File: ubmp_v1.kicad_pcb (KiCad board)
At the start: 2 copper layers, 33.5 x 14 mm, 26 parts, among them J1 Conn_02x05_Counter_Clockwise, J2 USB_A, U1 NUF8401MNT4G, U2 MIC5245-3.3, U3 STM32F103CBUx, U4 NUF2042XV6T1G, Y1 PRQC8.00CR1010V00L

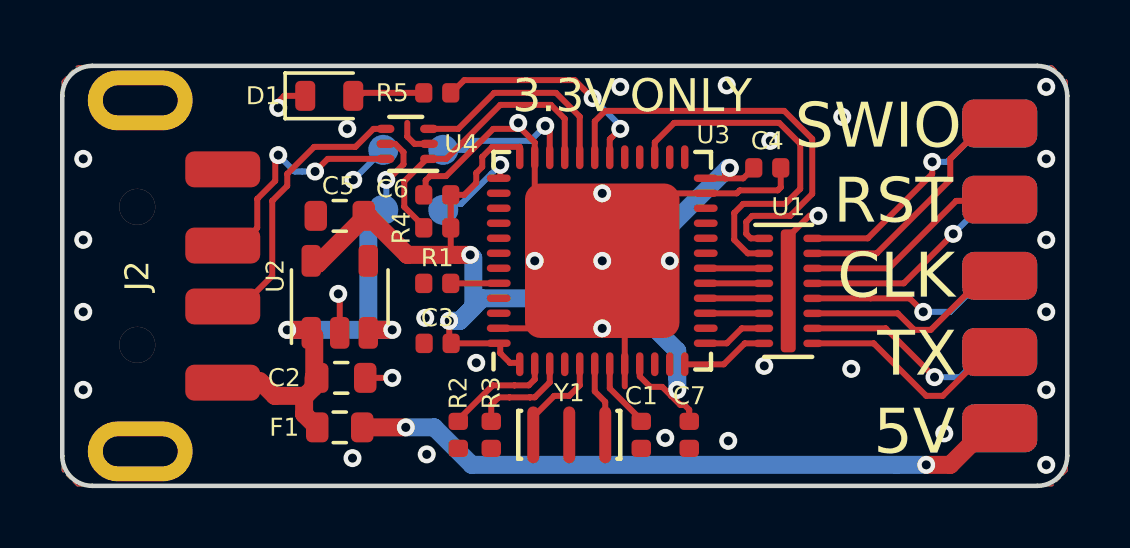
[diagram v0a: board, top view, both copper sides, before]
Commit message: Updated components + libs and changed to 1.5k resistor arrary
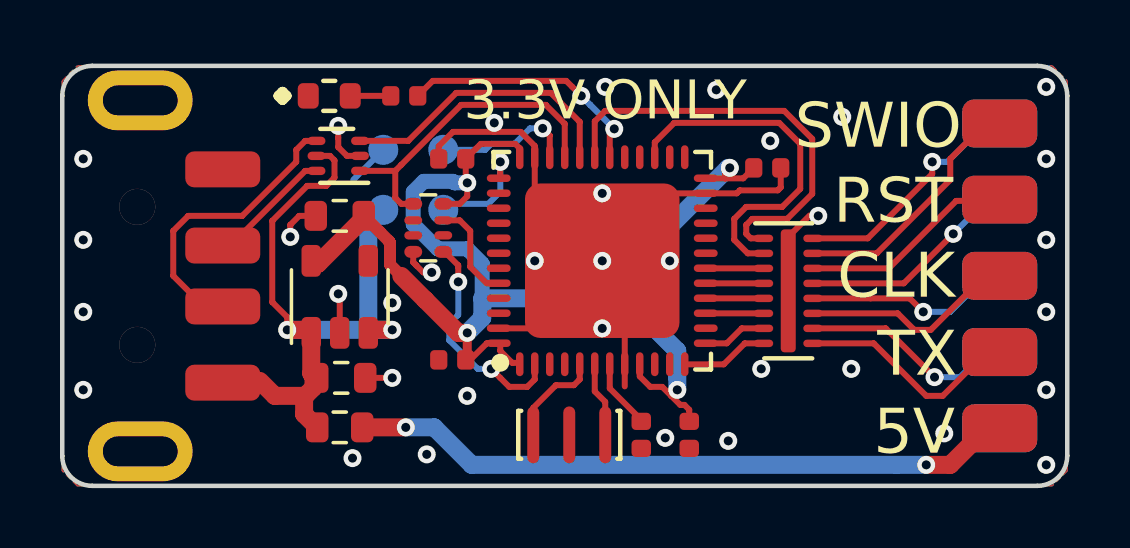
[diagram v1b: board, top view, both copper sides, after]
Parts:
- removed the R1 at (97.5, 106.2)
- removed R2, R3, R4: 1.5k, passive:R_0402_1005Metric_Rounded
- removed REF**: OSHW-Logo2_9.8x8mm_SilkScreen, Symbol:OSHW-Logo2_9.8x8mm_SilkScreen
- added RN1: 1.5k, passive:R_Array_Convex_4x0402, F.Cu at (97.2, 104.4)
- D1: footprint passive:D_0603_1608Metric_Rounded -> leds:LEDC1608X60
- moved U4 2.33 mm to (94.2, 102.0)
- moved C6 1.30 mm to (98.0, 102.1)
- moved R1 1.10 mm to (96.4, 100.0)
- moved C3 0.73 mm to (98.0, 108.8)
- renumbered R5 to R1
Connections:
- U3 pad 3: /bmp_core/STM_ID2 -> Net-(U3-Pad3)
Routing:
- net +5V: track 17.8 -> 22.6 mm, vias 3 -> 2
- net +3V3: track 40.2 -> 44.3 mm
- net /DP: track 8.19 -> 4.16 mm, vias 2 -> 0
- net /bmp_core/STM_ID: track 3.61 -> 7.43 mm, vias 0 -> 2
- net /bmp_core/STM_ID2: track 3.40 -> 0.00 mm
- net /bmp_core/DM_P: track 7.26 -> 9.57 mm
- net /bmp_core/LED_STLINK: track 7.82 -> 9.94 mm
- net /bmp_core/BOOT0: track 1.70 -> 3.42 mm
- net /bmp_core/DP_P: track 9.67 -> 10.7 mm
- net Net-(D1-Pad2): track 2.15 -> 1.25 mm
- net /bmp_core/SWCLK: track 2.89 -> 3.62 mm

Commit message: Minor PCB fixes, added OSHW logo
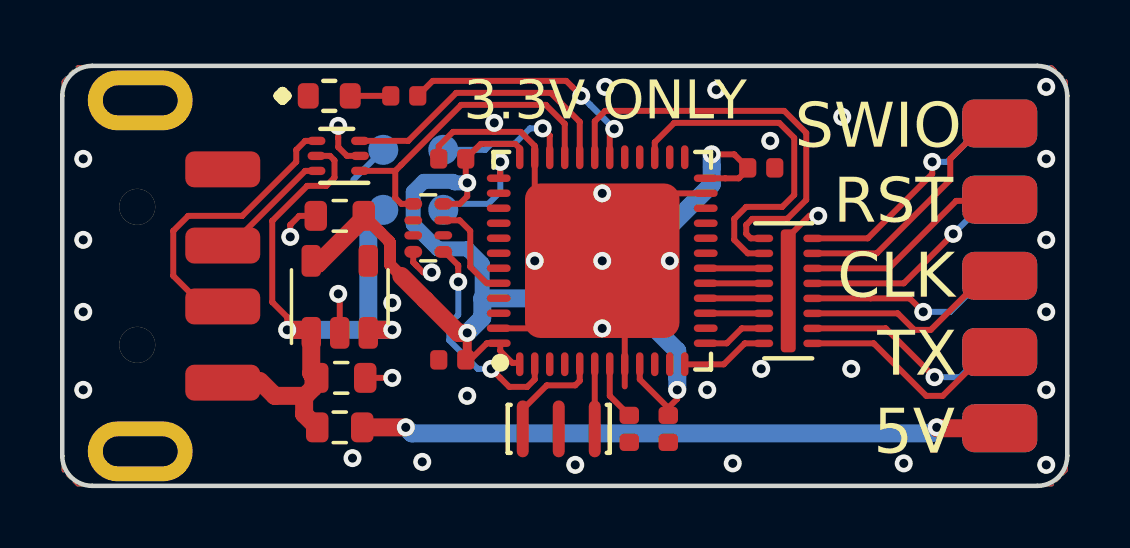
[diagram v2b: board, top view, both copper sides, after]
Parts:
- added REF**: OSHW-Symbol_6.7x6mm_SilkScreen, Symbol:OSHW-Symbol_6.7x6mm_SilkScreen, B.Cu at (106.1, 102.7)
- moved C7 0.73 mm to (105.2, 111.1)
- moved C1 0.45 mm to (103.9, 111.1)
- moved Y1 0.40 mm to (101.5, 111.1)
- moved C4 0.20 mm to (108.3, 102.4)
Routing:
- net GND: track 36.1 -> 32.9 mm, vias 35 -> 36
- net Net-(F1-Pad1): track 22.3 -> 21.4 mm

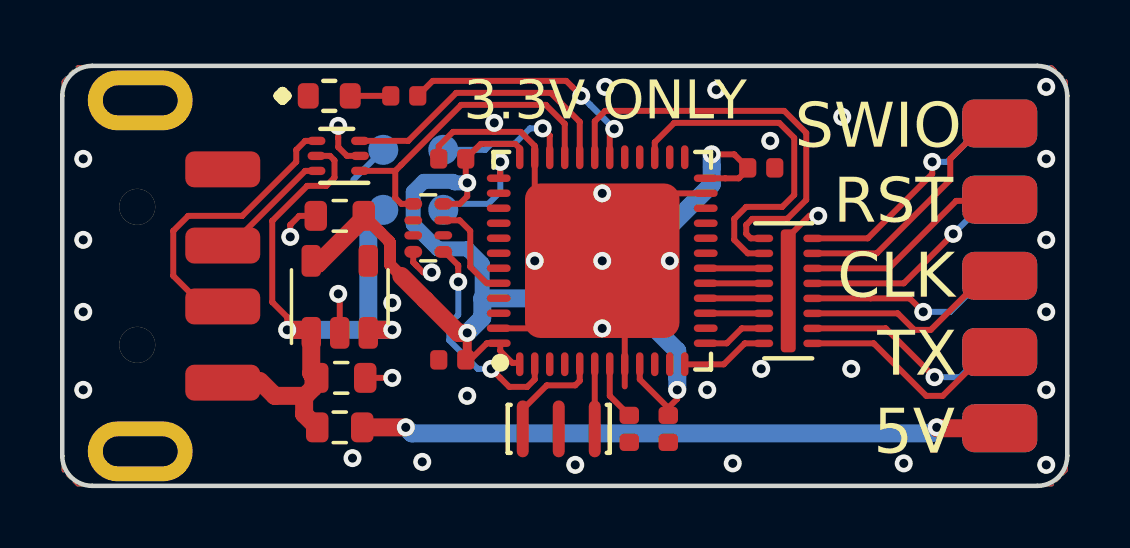
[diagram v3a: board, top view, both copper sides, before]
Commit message: Improved ground layout
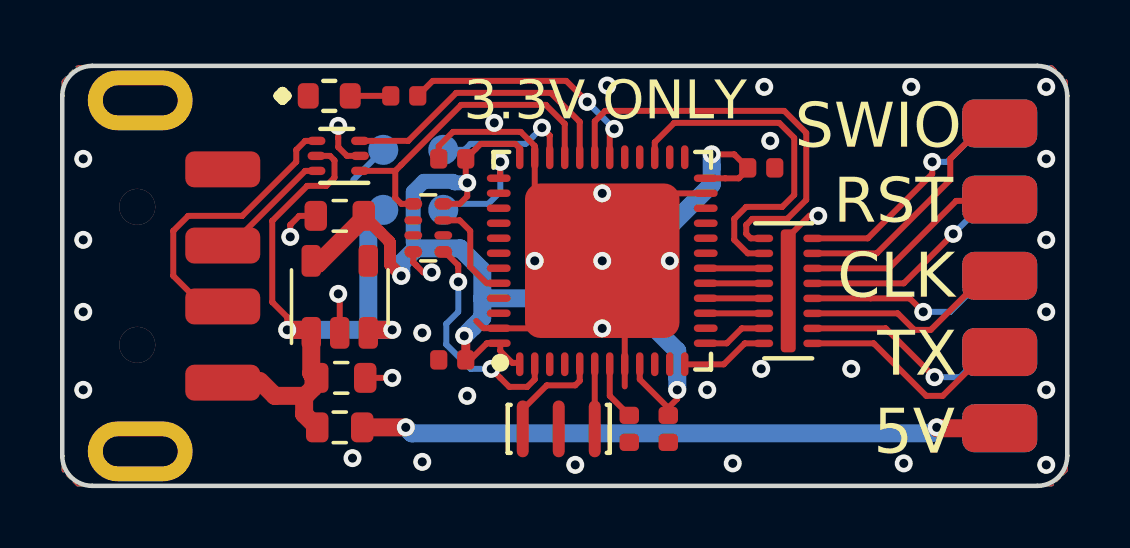
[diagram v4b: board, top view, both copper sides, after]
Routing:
- net +3V3: track 44.4 -> 42.6 mm, vias 4 -> 5
- net GND: track 32.9 -> 33.8 mm

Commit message: Fixed through holes on USB connector to be NPTH
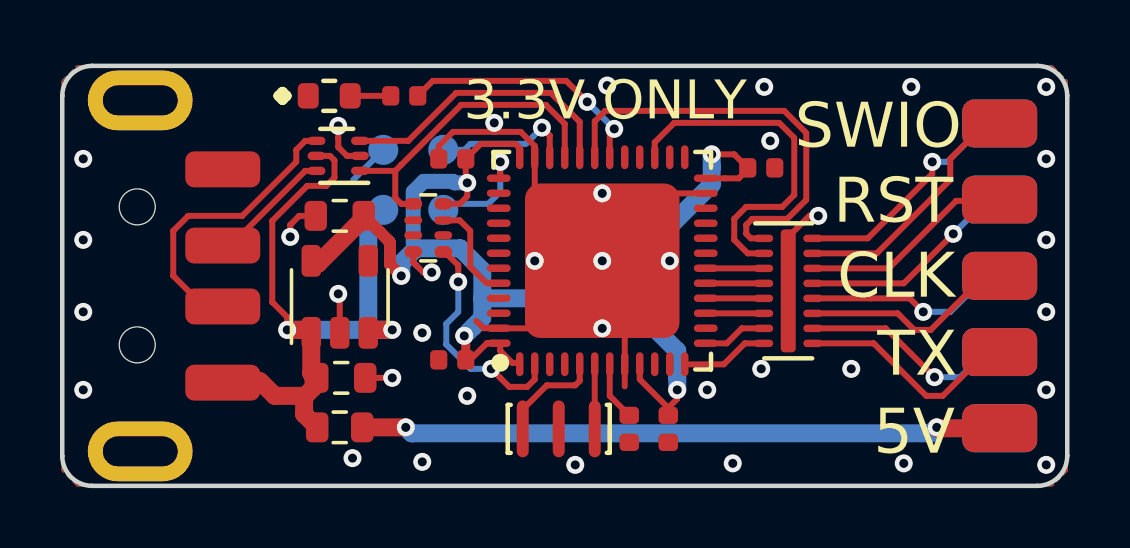
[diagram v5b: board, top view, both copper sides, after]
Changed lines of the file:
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@@
     (add_net +5V)
+  )
+  (module usb:USB_A_1001-011-01101 (layer F.Cu)
+    (at 89.6 106 270)
+    (descr "USB A connector, http://cdn-reichelt.de/documents/datenblatt/C100/USBAW%23ASS.pdf")
+    (tags "USB A")
+    (fp_text reference J2 (at 0 2.1 270) (layer F.SilkS) hide
+      (effects (font (size 0.8 0.8) (thickness 0.15)))
+    )
+    (fp_text value USB_A (at 3.55 15.1 270) (layer F.Fab)
+      (effects (font (size 1 1) (thickness 0.15)))
+    )
+    (fp_text user "PCB edge" (at 0.2 4 270) (layer Dwgs.User)
+      (effects (font (size 0.5 0.5) (thickness 0.075)))
+    )
+    (fp_text user %R (at -0.1 2.8 270) (layer F.Fab)
+      (effects (font (size 1 1) (thickness 0.15)))
+    )
+    (fp_line (start 6.6 4.6) (end -6.7 4.6) (layer Dwgs.User) (width 0.12))
+    (fp_line (start -5.5 -1.05) (end -6.7 0.15) (layer F.Fab) (width 0.15))
+    (fp_line (start 6.6 -1.05) (end -5.5 -1.05) (layer F.Fab) (width 0.15))
+    (fp_line (start 6.6 20) (end 6.6 -1.05) (layer F.Fab) (width 0.15))
+    (fp_line (start -6.7 20) (end 6.6 20) (layer F.Fab) (width 0.15))
+    (fp_line (start -6.7 0.15) (end -6.7 20) (layer F.Fab) (width 0.15))
+    (fp_line (start -7.1 -2.2) (end 7.1 -2.2) (layer F.CrtYd) (width 0.05))
+    (fp_line (start -7.1 -2.2) (end -7.1 13.2) (layer F.CrtYd) (width 0.05))
+    (fp_line (start 7.1 13.2) (end 7.1 -2.2) (layer F.CrtYd) (width 0.05))
+    (fp_line (start 7.1 13.2) (end -7.1 13.2) (layer F.CrtYd) (width 0.05))
+    (pad "" np_thru_hole circle (at -2.3 2.1 180) (size 1.2 1.2) (drill 1.2) (layers *.Cu *.Mask))
+    (pad "" np_thru_hole circle (at 2.3 2.1 180) (size 1.2 1.2) (drill 1.2) (layers *.Cu *.Mask))
+    (pad 1 smd roundrect (at 3.56 -0.75 180) (size 2.5 1.2) (layers F.Cu F.Mask)(roundrect_rratio 0.25)
+      (net 3 +5V))
+    (pad 2 smd roundrect (at 1.02 -0.75 180) (size 2.5 1.2) (layers F.Cu F.Mask)(roundrect_rratio 0.25)
+      (net 4 /DM))
+    (pad 3 smd roundrect (at -1.01 -0.75 180) (size 2.5 1.2) (layers F.Cu F.Mask)(roundrect_rratio 0.25)
+      (net 5 /DP))
+    (pad 4 smd roundrect (at -3.55 -0.75 180) (size 2.5 1.2) (layers F.Cu F.Mask)(roundrect_rratio 0.25)
+      (net 2 GND))
+    (pad 5 thru_hole oval (at 5.85 2 180) (size 3.5 2) (drill oval 2.5 1) (layers *.Cu *.Mask)
+      (net 2 GND))
+    (pad 5 thru_hole oval (at -5.85 2 180) (size 3.5 2) (drill oval 2.5 1) (layers *.Cu *.Mask)
+      (net 2 GND))
+    (model ${KIPRJMOD}/kicad_libs/3dmodels/step/1001-011-01101.step
+      (offset (xyz 0 -19.6 0.9))
+      (scale (xyz 1 1 1))
+      (rotate (xyz 0 -180 0))
+    )
   )
   (module passive:R_Array_Convex_4x0402 (layer F.Cu)
@@
     )
   )
-  (module usb:USB_A_1001-011-01101 (layer F.Cu)
-    (at 89.6 106 270)
-    (descr "USB A connector, http://cdn-reichelt.de/documents/datenblatt/C100/USBAW%23ASS.pdf")
-    (tags "USB A")
-    (fp_text reference J2 (at 0 2.1 270) (layer F.SilkS) hide
-      (effects (font (size 0.8 0.8) (thickness 0.15)))
-    )
-    (fp_text value USB_A (at 3.55 15.1 270) (layer F.Fab)
-      (effects (font (size 1 1) (thickness 0.15)))
-    )
-    (fp_text user "PCB edge" (at 0.2 4 270) (layer Dwgs.User)
-      (effects (font (size 0.5 0.5) (thickness 0.075)))
-    )
-    (fp_text user %R (at -0.1 2.8 270) (layer F.Fab)
-      (effects (font (size 1 1) (thickness 0.15)))
-    )
-    (fp_line (start 6.6 4.6) (end -6.7 4.6) (layer Dwgs.User) (width 0.12))
-    (fp_line (start -5.5 -1.05) (end -6.7 0.15) (layer F.Fab) (width 0.15))
-    (fp_line (start 6.6 -1.05) (end -5.5 -1.05) (layer F.Fab) (width 0.15))
-    (fp_line (start 6.6 20) (end 6.6 -1.05) (layer F.Fab) (width 0.15))
-    (fp_line (start -6.7 20) (end 6.6 20) (layer F.Fab) (width 0.15))
-    (fp_line (start -6.7 0.15) (end -6.7 20) (layer F.Fab) (width 0.15))
-    (fp_line (start -7.1 -2.2) (end 7.1 -2.2) (layer F.CrtYd) (width 0.05))
-    (fp_line (start -7.1 -2.2) (end -7.1 13.2) (layer F.CrtYd) (width 0.05))
-    (fp_line (start 7.1 13.2) (end 7.1 -2.2) (layer F.CrtYd) (width 0.05))
-    (fp_line (start 7.1 13.2) (end -7.1 13.2) (layer F.CrtYd) (width 0.05))
-    (pad 7 thru_hole circle (at -2.3 2.1 180) (size 1.2 1.2) (drill 1.2) (layers *.Cu *.Mask))
-    (pad 6 thru_hole circle (at 2.3 2.1 180) (size 1.2 1.2) (drill 1.2) (layers *.Cu *.Mask))
-    (pad 1 smd roundrect (at 3.56 -0.75 180) (size 2.5 1.2) (layers F.Cu F.Mask)(roundrect_rratio 0.25)
-      (net 3 +5V))
-    (pad 2 smd roundrect (at 1.02 -0.75 180) (size 2.5 1.2) (layers F.Cu F.Mask)(roundrect_rratio 0.25)
-      (net 4 /DM))
-    (pad 3 smd roundrect (at -1.01 -0.75 180) (size 2.5 1.2) (layers F.Cu F.Mask)(roundrect_rratio 0.25)
-      (net 5 /DP))
-    (pad 4 smd roundrect (at -3.55 -0.75 180) (size 2.5 1.2) (layers F.Cu F.Mask)(roundrect_rratio 0.25)
-      (net 2 GND))
-    (pad 5 thru_hole oval (at 5.85 2 180) (size 3.5 2) (drill oval 2.5 1) (layers *.Cu *.Mask)
-      (net 2 GND))
-    (pad 5 thru_hole oval (at -5.85 2 180) (size 3.5 2) (drill oval 2.5 1) (layers *.Cu *.Mask)
-      (net 2 GND))
-    (model ${KIPRJMOD}/kicad_libs/3dmodels/step/1001-011-01101.step
-      (offset (xyz 0 -19.6 0.9))
-      (scale (xyz 1 1 1))
-      (rotate (xyz 0 -180 0))
-    )
-  )

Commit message: Updated part numbers
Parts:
- removed REF**: OSHW-Symbol_6.7x6mm_SilkScreen, Symbol:OSHW-Symbol_6.7x6mm_SilkScreen
- D1: value GREEN -> LTST-C191KGKT
- J1: value Conn_02x05_Counter_Clockwise -> M20-9760542
- J2: value USB_A -> 1001-011-01101
- RN1: value 1.5k -> EXB-28V152JX
- U2: value MIC5245-3.3 -> MIC5245-3.3YM5
- U3: value STM32F103CBUx -> STM32F103CBU6
